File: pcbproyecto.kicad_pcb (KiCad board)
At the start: 4 copper layers, 75 x 108 mm, 21 parts, among them J1 Barrel_Jack_Switch, J2 Conn_02x20_Odd_Even, J3 Micro_SD_Card, J4 USB_A, J5 Conn_01x01_Male, P1 USB_C_Plug_USB2.0, U1 LM2576HVS-5, U2 LM117_TO3, U3 OSD3358-512M-BSM

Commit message: Progress
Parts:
- removed J5: Conn_01x01_Male, Connector_PinHeader_1.00mm:PinHeader_1x01_P1.00mm_Vertical
- added H1: MGT, MountingHole:MountingHole_3.2mm_M3, F.Cu at (81.3, 120.0)
- added H2: MGT, MountingHole:MountingHole_3.2mm_M3, F.Cu at (19.1, 119.0)
- added H3: MGT, MountingHole:MountingHole_3.2mm_M3, F.Cu at (17.9, 23.8)
- added H4: MGT, MountingHole:MountingHole_3.2mm_M3, F.Cu at (81.4, 23.9)
- added LED1: L_PWR, LED_SMD:LED_0603_1608Metric, F.Cu at (72.3, 71.9)
- added PWR1: PSH_BTN, footprints:MINI_PUSHBUTTON, F.Cu at (77.3, 71.1)
- added Q1: MMBT3906, Package_TO_SOT_SMD:SOT-23, F.Cu at (92.1, 99.8)
- added Q2: MMBT3906, Package_TO_SOT_SMD:SOT-23, F.Cu at (50.4, 38.2)
- added R1: 1K, Resistor_SMD:R_0603_1608Metric, F.Cu at (72.3, 67.7)
- added R2: 0.1 5%, Resistor_SMD:R_0603_1608Metric, F.Cu at (95.7, 100.0)
- added R3: R, Resistor_SMD:R_0603_1608Metric, F.Cu at (98.2, 100.0)
- added R4: R, Resistor_SMD:R_0603_1608Metric, F.Cu at (95.7, 96.0)
- added R5: R, Resistor_SMD:R_0603_1608Metric, F.Cu at (91.1, 91.1)
- added R6: R, Resistor_SMD:R_0603_1608Metric, F.Cu at (60.4, 39.9)
- added R7: R, Resistor_SMD:R_0603_1608Metric, F.Cu at (60.3, 36.3)
- added R8: R, Resistor_SMD:R_0603_1608Metric, F.Cu at (53.8, 38.2)
- added RST1: PSH_BTN, footprints:MINI_PUSHBUTTON, F.Cu at (77.3, 64.3)
- added TP1: TP_PWR_EN, TestPoint:TestPoint_Pad_1.0x1.0mm, F.Cu at (74.6, 56.8)
- added TP2: TP_PWRONSTN, TestPoint:TestPoint_Pad_1.0x1.0mm, F.Cu at (77.6, 56.8)
- added TP3: TP_WAKEUP, TestPoint:TestPoint_Pad_1.0x1.0mm, F.Cu at (74.6, 53.7)
- added TP4: TP_EXTINTN, TestPoint:TestPoint_Pad_1.0x1.0mm, F.Cu at (77.6, 53.7)
- added TP5: TP_I2C_SCL, TestPoint:TestPoint_Pad_1.0x1.0mm, F.Cu at (74.6, 50.7)
- added TP6: TP_I2C_SDA, TestPoint:TestPoint_Pad_1.0x1.0mm, F.Cu at (77.6, 50.7)
- added TP7: TP_VIN_BAT, TestPoint:TestPoint_Pad_1.0x1.0mm, F.Cu at (74.6, 47.6)
- added U4: TLVH431, Package_TO_SOT_SMD:SOT-23, F.Cu at (92.1, 95.3)
- added U5: TLVH431, Package_TO_SOT_SMD:SOT-23, F.Cu at (57.0, 38.2)
- C1: value 100u -> 100uF
- moved J2 19.3 mm to (35.9, 27.1), turned to 90 degrees
- turned U3 to 0 degrees
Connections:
- J2 pad 1: /UART_TX -> /Interfaces/UART_TX
- J2 pad 3: /UART_RX -> /Interfaces/UART_RX
- U3 pad A7: /Sistem In Package/ADC_VREF+ -> Net-(U3-PadA7)
- U3 pad A9: /Sistem In Package/ADC_VREF- -> Net-(U3-PadA9)
- U3 pad B7: /Sistem In Package/ADC_VREF+ -> Net-(U3-PadB7)
- U3 pad B9: /Sistem In Package/ADC_VREF- -> Net-(U3-PadB9)
- U3 pad C10: Net-(U3-PadC10) -> Net-(TP5-Pad1)
- U3 pad C11: Net-(U3-PadC11) -> Net-(TP6-Pad1)
- U3 pad D10: Net-(U3-PadD10) -> Net-(TP5-Pad1)
- U3 pad D11: Net-(U3-PadD11) -> Net-(TP6-Pad1)
- U3 pad D4: Net-(U3-PadD4) -> Net-(TP4-Pad1)
- U3 pad D8: Net-(U3-PadD8) -> GND
- U3 pad D9: Net-(U3-PadD9) -> GND
- U3 pad E10: Net-(U3-PadE10) -> GND
- U3 pad E11: Net-(U3-PadE11) -> GND
- U3 pad E12: Net-(U3-PadE12) -> GND
- U3 pad E4: Net-(U3-PadE4) -> Net-(TP4-Pad1)
- U3 pad E5: Net-(U3-PadE5) -> GND
- U3 pad E6: Net-(U3-PadE6) -> GND
- U3 pad E7: Net-(U3-PadE7) -> GND
- U3 pad E8: Net-(U3-PadE8) -> GND
- U3 pad E9: Net-(U3-PadE9) -> GND
- U3 pad F12: Net-(U3-PadF12) -> GND
- U3 pad F5: Net-(U3-PadF5) -> GND
- U3 pad G12: Net-(U3-PadG12) -> GND
- U3 pad G5: Net-(U3-PadG5) -> GND
- U3 pad H12: Net-(U3-PadH12) -> GND
- U3 pad H13: Net-(U3-PadH13) -> GND
- U3 pad H4: Net-(U3-PadH4) -> GND
- U3 pad H5: Net-(U3-PadH5) -> GND
- U3 pad J12: Net-(U3-PadJ12) -> GND
- U3 pad J13: Net-(U3-PadJ13) -> GND
- U3 pad J4: Net-(U3-PadJ4) -> GND
- U3 pad J5: Net-(U3-PadJ5) -> GND
- U3 pad K12: Net-(U3-PadK12) -> GND
- U3 pad K5: Net-(U3-PadK5) -> GND
- U3 pad L12: Net-(U3-PadL12) -> GND
- U3 pad L4: Net-(U3-PadL4) -> Net-(TP3-Pad1)
- U3 pad L5: Net-(U3-PadL5) -> GND
- U3 pad M10: Net-(U3-PadM10) -> GND
- U3 pad M11: Net-(U3-PadM11) -> GND
- U3 pad M12: Net-(U3-PadM12) -> GND
- U3 pad M4: Net-(U3-PadM4) -> Net-(TP3-Pad1)
- U3 pad M5: Net-(U3-PadM5) -> GND
- U3 pad M6: Net-(U3-PadM6) -> GND
- U3 pad M7: Net-(U3-PadM7) -> GND
- U3 pad M8: Net-(U3-PadM8) -> GND
- U3 pad M9: Net-(U3-PadM9) -> GND
- U3 pad N10: Net-(U3-PadN10) -> Net-(TP1-Pad1)
- U3 pad N11: Net-(U3-PadN11) -> Net-(TP1-Pad1)
- U3 pad N4: Net-(U3-PadN4) -> Net-(TP2-Pad1)
- U3 pad N5: Net-(U3-PadN5) -> Net-(TP2-Pad1)
- U3 pad N8: Net-(U3-PadN8) -> GND
- U3 pad N9: Net-(U3-PadN9) -> GND
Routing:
- net +3V3: track 197.8 -> 164.8 mm
- net /UART_TX: track 0.00 -> 33.0 mm
- net /UART_RX: track 0.00 -> 30.6 mm
- net VDD_5V: track 17.5 -> 0.00 mm, vias 0 -> 3
- net GND: track 404.3 -> 408.8 mm, vias 10 -> 18
- net Net-(U3-PadC14): track 0.00 -> 4.42 mm
- net Net-(U3-PadB15): track 0.00 -> 3.11 mm
- net Net-(U3-PadA15): track 0.00 -> 3.10 mm
- net Net-(U3-PadB14): track 0.00 -> 3.04 mm
- net Net-(U3-PadB13): track 0.00 -> 3.00 mm
- net Net-(U3-PadA16): track 0.00 -> 1.62 mm
- net Net-(U3-PadB16): track 0.00 -> 1.58 mm
- net Net-(U3-PadA14): track 0.00 -> 1.57 mm
- net Net-(TP2-Pad1): track 0.00 -> 1.27 mm
- net VDD_3V3A: track 0.00 -> 1.27 mm, vias 0 -> 3
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- added copper zone on F.Cu, net GND
- added copper zone on GND.Cu, net GND
- added copper zone on F.Cu, net USB_DC
- added copper zone on F.Cu, net VDD_3V3A
- added copper zone on F.Cu, net VDD_5V
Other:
- rule via_min_drill: 0.3048 -> 0.2
- rule via_min_size: 0.6096 -> 0.3048

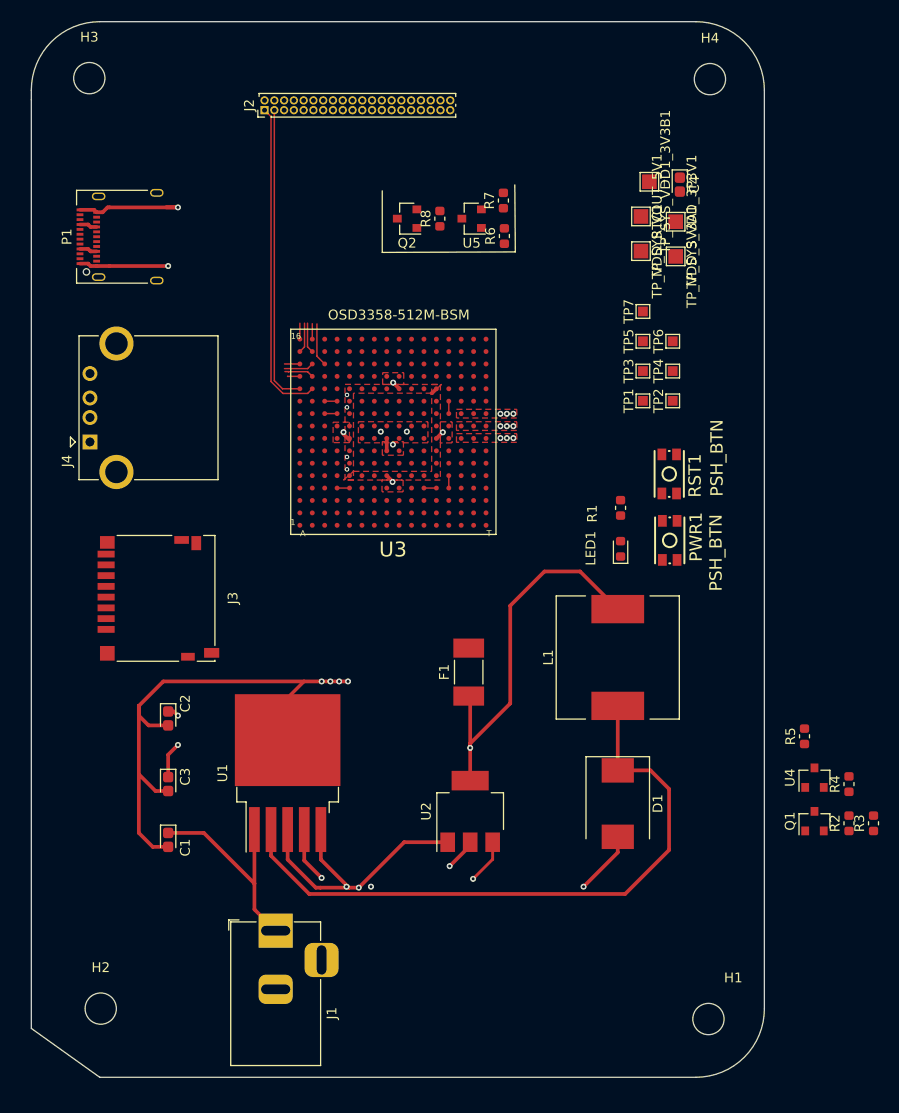
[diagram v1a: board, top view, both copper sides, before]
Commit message: EMD Protection
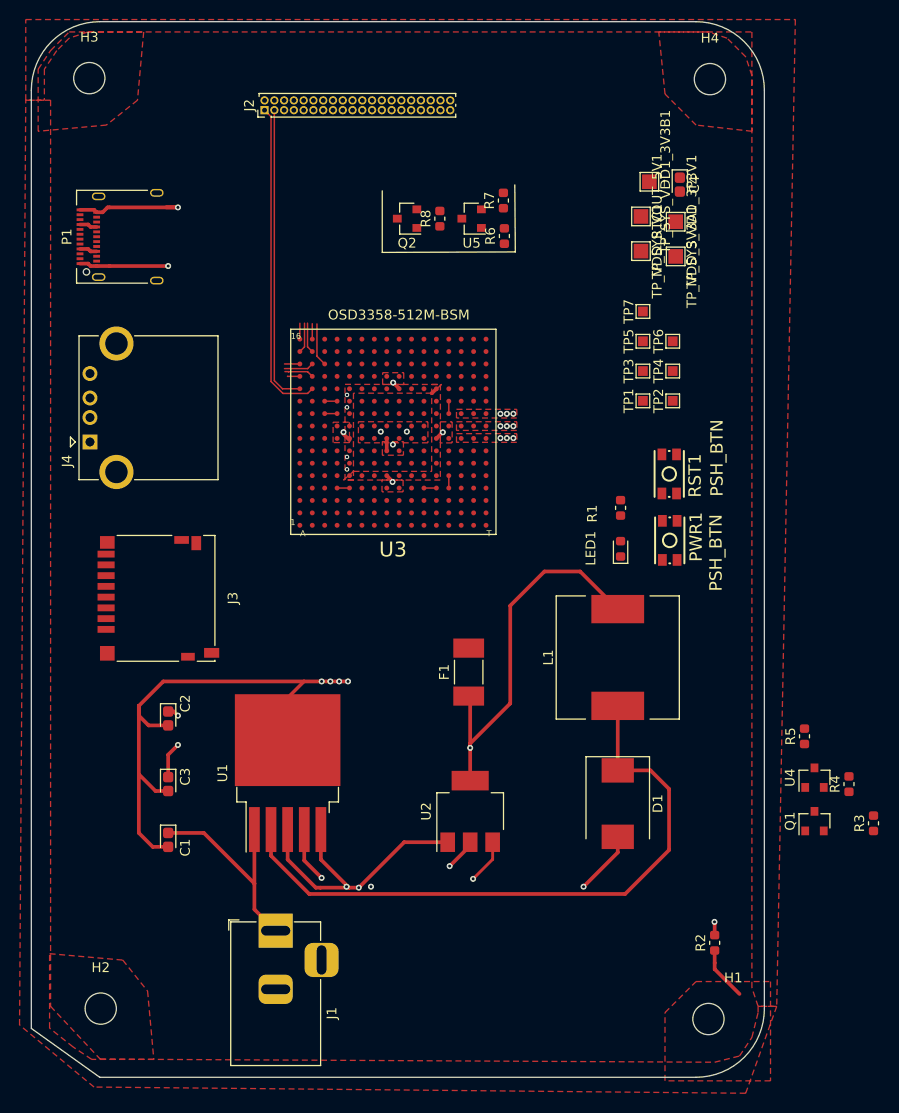
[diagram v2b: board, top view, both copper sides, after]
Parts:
- moved R2 18.4 mm to (81.9, 112.2)
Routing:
- net GND: track 408.8 -> 425.0 mm, vias 18 -> 19
- net CGND: track 0.00 -> 5.50 mm
- added copper zone on F.Cu, net CGND
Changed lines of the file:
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@@
     (thickness 1.6)
     (drawings 12)
-    (tracks 215)
+    (tracks 225)
     (zones 0)
     (modules 46)
@@
   )
   (setup
-    (last_trace_width 0.1524)
+    (last_trace_width 0.381)
     (user_trace_width 0.1524)
     (user_trace_width 0.381)
@@
   )
   (module Resistor_SMD:R_0603_1608Metric (layer F.Cu)
-    (at 95.6576 100.0144 90)
+    (at 81.915 112.2425 90)
     (descr "Resistor SMD 0603 (1608 Metric), square (rectangular) end terminal, IPC_7351 nominal, (Body size source: http://www.tortai-tech.com/upload/download/2011102023233369053.pdf), generated with kicad-footprint-generator")
     (tags resistor)
@@
       (effects (font (size 1 1) (thickness 0.15)))
     )
-    (fp_text value "0.1 5%" (at 0 1.43 90) (layer F.Fab)
+    (fp_text value "0.1 5%" (at 0 1.43 270) (layer F.Fab)
       (effects (font (size 1 1) (thickness 0.15)))
     )
@@
   (via (at 44.2976 62.5348) (size 0.4572) (drill 0.254) (layers F.Cu B.Cu) (net 1))
   (via (at 44.2976 63.8048) (size 0.4572) (drill 0.254) (layers F.Cu B.Cu) (net 1))
+  (segment (start 81.915 111.455) (end 81.915 110.315) (width 0.381) (layer F.Cu) (net 1))
+  (segment (start 81.915 110.315) (end 81.915 110.115) (width 0.381) (layer F.Cu) (net 1))
+  (via (at 81.9 110.1) (size 0.6096) (drill 0.3048) (layers F.Cu B.Cu) (net 1))
+  (segment (start 81.915 110.115) (end 81.9 110.1) (width 0.381) (layer F.Cu) (net 1))
+  (segment (start 68.5 106.6) (end 78.3 106.6) (width 0.381) (layer GND.Cu) (net 1))
+  (segment (start 78.4 106.6) (end 81.9 110.1) (width 0.381) (layer GND.Cu) (net 1))
+  (segment (start 78.3 106.6) (end 78.4 106.6) (width 0.381) (layer GND.Cu) (net 1))
   (segment (start 34.825 108.825) (end 38 112) (width 0.381) (layer F.Cu) (net 2))
   (segment (start 29.65 101) (end 34.825 106.175) (width 0.381) (layer F.Cu) (net 2))
@@
   (segment (start 42.015 58.09754) (end 43.285 58.09754) (width 0.1524) (layer F.Cu) (net 245))
   (segment (start 42.015 56.82754) (end 43.285 56.82754) (width 0.1524) (layer F.Cu) (net 246))
+  (segment (start 81.915 113.03) (end 81.915 114.3) (width 0.381) (layer F.Cu) (net 255))
+  (segment (start 81.915 114.3) (end 81.915 114.935) (width 0.381) (layer F.Cu) (net 255))
+  (segment (start 81.915 114.935) (end 84.455 117.475) (width 0.381) (layer F.Cu) (net 255))
   (zone (net 1) (net_name GND) (layer F.Cu) (hatch edge 0.508)
     (connect_pads yes (clearance 0.508))
@@
       )
     )
+  )
+  (zone (net 255) (net_name CGND) (layer F.Cu) (hatch edge 0.508)
+    (connect_pads yes (clearance 0.508))
+    (min_thickness 0.254)
+    (fill yes (arc_segments 32) (thermal_gap 0.508) (thermal_bridge_width 0.508))
+    (polygon
+      (pts
+        (xy 13.97 118.745) (xy 19.05 124.1425) (xy 81.915 124.46) (xy 84.455 123.825) (xy 85.725 121.92)
+        (xy 86.36 119.38) (xy 86.36 118.745) (xy 88.265 118.745) (xy 85.09 127.635) (xy 18.415 127)
+        (xy 10.795 120.65) (xy 11.43 26.035) (xy 13.97 26.035)
+      )
+    )
+  )
+  (zone (net 255) (net_name CGND) (layer F.Cu) (hatch edge 0.508)
+    (connect_pads yes (clearance 0.508))
+    (min_thickness 0.254)
+    (fill yes (arc_segments 32) (thermal_gap 0.508) (thermal_bridge_width 0.508))
+    (polygon
+      (pts
+        (xy 88.265 118.745) (xy 86.36 118.745) (xy 85.725 116.84) (xy 85.725 23.495) (xy 85.09 21.59)
+        (xy 83.185 19.685) (xy 81.28 19.05) (xy 17.78 19.05) (xy 15.875 19.685) (xy 14.605 20.955)
+        (xy 13.335 22.86) (xy 13.335 26.035) (xy 11.43 26.035) (xy 11.43 17.78) (xy 90.17 17.78)
+      )
+    )
+  )
+  (zone (net 255) (net_name CGND) (layer F.Cu) (hatch edge 0.508)
+    (connect_pads yes (clearance 0.508))
+    (min_thickness 0.254)
+    (fill yes (arc_segments 32) (thermal_gap 0.508) (thermal_bridge_width 0.508) (smoothing fillet) (radius 5))
+    (polygon
+      (pts
+        (xy 22.86 26.035) (xy 19.685 28.575) (xy 12.7 29.21) (xy 12.7 22.86) (xy 13.97 20.955)
+        (xy 15.875 19.05) (xy 23.495 19.05)
+      )
+    )
+  )
+  (zone (net 255) (net_name CGND) (layer F.Cu) (hatch edge 0.508)
+    (connect_pads yes (clearance 0.508))
+    (min_thickness 0.254)
+    (fill yes (arc_segments 32) (thermal_gap 0.508) (thermal_bridge_width 0.508) (smoothing fillet) (radius 5))
+    (polygon
+      (pts
+        (xy 85.725 29.21) (xy 80.01 28.575) (xy 76.835 25.4) (xy 76.2 19.05) (xy 85.725 19.05)
+      )
+    )
+  )
+  (zone (net 255) (net_name CGND) (layer F.Cu) (hatch edge 0.508)
+    (connect_pads yes (clearance 0.508))
+    (min_thickness 0.254)
+    (fill yes (arc_segments 32) (thermal_gap 0.508) (thermal_bridge_width 0.508) (smoothing fillet) (radius 5))
+    (polygon
+      (pts
+        (xy 76.835 126.365) (xy 76.835 119.38) (xy 80.01 116.205) (xy 87.63 116.205) (xy 87.63 126.365)
+      )
+    )
+  )
+  (zone (net 255) (net_name CGND) (layer F.Cu) (hatch edge 0.508)
+    (connect_pads yes (clearance 0.508))
+    (min_thickness 0.254)
+    (fill yes (arc_segments 32) (thermal_gap 0.508) (thermal_bridge_width 0.508) (smoothing fillet) (radius 5))
+    (polygon
+      (pts
+        (xy 21.355229 114.009418) (xy 23.895229 117.184418) (xy 24.530229 124.169418) (xy 18.180229 124.169418) (xy 16.275229 122.899418)
+        (xy 13.8684 120.97512) (xy 13.8684 113.35512)
+      )
+    )

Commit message: Progress
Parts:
- removed J2: Conn_02x20_Odd_Even, Connector_PinHeader_1.00mm:PinHeader_2x20_P1.00mm_Vertical
- removed J4: USB_A, Connector_USB:USB_A_CONNFLY_DS1095-WNR0
- removed P1: USB_C_Plug_USB2.0, Connector_USB:USB_C_Receptacle_Amphenol_12401610E4-2A
- removed the R1 at (72.3, 67.7)
- removed RST1: PSH_BTN, footprints:MINI_PUSHBUTTON
- removed TP1: TP_PWR_EN, TestPoint:TestPoint_Pad_1.0x1.0mm
- removed TP2: TP_PWRONSTN, TestPoint:TestPoint_Pad_1.0x1.0mm
- removed TP3: TP_WAKEUP, TestPoint:TestPoint_Pad_1.0x1.0mm
- removed TP4: TP_EXTINTN, TestPoint:TestPoint_Pad_1.0x1.0mm
- removed TP5: TP_I2C_SCL, TestPoint:TestPoint_Pad_1.0x1.0mm
- removed TP6: TP_I2C_SDA, TestPoint:TestPoint_Pad_1.0x1.0mm
- removed TP7: TP_VIN_BAT, TestPoint:TestPoint_Pad_1.0x1.0mm
- removed TP_SYS_VDD1_3V3B1, TP_SYS_VDD_3P3V1, TP_SYS_VOUT_5V1, TP_VDD_3V3A1, TP_VDD_RTC1: TestPoint, TestPoint:TestPoint_Pad_1.5x1.5mm
- added C5: 100uF, Capacitor_Tantalum_SMD:CP_EIA-1608-08_AVX-J, F.Cu at (30.7, 102.9)
- added C6: 100u, Capacitor_Tantalum_SMD:CP_EIA-1608-08_AVX-J, F.Cu at (30.7, 100.2)
- added C7: 1000u, Capacitor_Tantalum_SMD:CP_EIA-1608-08_AVX-J, F.Cu at (30.7, 97.5)
- added C8: 10uF, 10V, Capacitor_Tantalum_SMD:CP_EIA-1608-08_AVX-J, F.Cu at (62.0, 71.5)
- added C9: 0.1uF 6,3V, Capacitor_Tantalum_SMD:CP_EIA-1608-08_AVX-J, F.Cu at (62.0, 75.6)
- added IC1: SN74LVC1G07DCK, Package_TO_SOT_SMD:SOT-23-5, F.Cu at (73.2, 48.1)
- added J5: USB_B_Micro, Connector_USB:USB_Micro-B_Amphenol_10104110_Horizontal, F.Cu at (19.3, 56.5)
- added R2: R, Resistor_SMD:R_0603_1608Metric, F.Cu at (62.7, 33.7)
- added R22: 1K, Resistor_SMD:R_0603_1608Metric, F.Cu at (70.0, 34.8)
- added R23: 1M , 1%, Resistor_SMD:R_0603_1608Metric, F.Cu at (48.1, 27.0)
- added R9: 100K, pocketbeagle:RN0804, F.Cu at (44.6, 77.2)
- added RN1: 10K, pocketbeagle:RN0804, F.Cu at (34.5, 76.8)
- added RN2: 10K, pocketbeagle:RN0804, F.Cu at (34.5, 74.3)
- C1: value 100uF -> 0.1uF , 6.3V
- C2: value 1000u -> 18pF, 50V
- C3: value 100u -> 18pF, 50V
- J3: value Micro_SD_Card -> USB_A; footprint Connector_Card:microSD_HC_Hirose_DM3D-SF -> Connector_USB:USB_A_CONNFLY_DS1095-WNR0
- Q2: value MMBT3906 -> 24 MHz; footprint Package_TO_SOT_SMD:SOT-23 -> Crystal:Crystal_SMD_TXC_7A-2Pin_5x3.2mm
- R5: value R -> 10K
- R6, R7, R8: value R -> 100K; footprint Resistor_SMD:R_0603_1608Metric -> pocketbeagle:RN0804
- U1: value LM2576HVS-5 -> TLVH431; footprint Package_TO_SOT_SMD:TO-263-5_TabPin3 -> Package_TO_SOT_SMD:SOT-23
- U2: value LM117_TO3 -> OSD3358-512M-BSM; footprint Package_TO_SOT_SMD:SOT-223-3_TabPin2 -> footprints:OSD335X-BGA-256
- U3: value OSD3358-512M-BSM -> LM117_TO3; footprint footprints:OSD335X-BGA-256 -> Package_TO_SOT_SMD:SOT-223-3_TabPin2
- U4: value TLVH431 -> LM2576HVS-5; footprint Package_TO_SOT_SMD:SOT-23 -> Package_TO_SOT_SMD:TO-263-5_TabPin3
- U5: value TLVH431 -> MICROSD; footprint Package_TO_SOT_SMD:SOT-23 -> pocketbeagle:MICROSD
- moved R3 78.1 mm to (62.7, 30.4), turned to 0 degrees
- moved Q1 77.7 mm to (67.5, 26.1), turned to 0 degrees
- moved R4 76.5 mm to (62.7, 27.0), turned to 0 degrees
- moved C1 75.0 mm to (78.7, 48.4), turned to 90 degrees
- moved C3 68.5 mm to (48.1, 31.2), turned to 180 degrees
- moved R5 67.3 mm to (48.2, 39.2), turned to 180 degrees
- moved U1 66.2 mm to (56.2, 31.2), turned to 0 degrees
- moved C2 59.1 mm to (48.2, 34.5), turned to 180 degrees
- moved C4 53.3 mm to (34.1, 64.5), turned to 90 degrees
- moved U5 47.3 mm to (29.7, 76.7)
- moved R7 41.3 mm to (53.0, 76.9), turned to 0 degrees
- moved U4 39.8 mm to (52.4, 98.0)
- moved R8 39.6 mm to (47.4, 77.2), turned to 0 degrees
- moved J3 39.1 mm to (28.2, 38.0)
- moved R6 37.2 mm to (56.0, 76.9), turned to 0 degrees
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- renumbered R2 to R1
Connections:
- C1 pad 1: /Power Suply/in_pwr_supply -> GND
- C1 pad 2: GND -> VDD_RTC
- C2 pad 1: +5V -> /Sistem In Package/OSC_OUT
- C2 pad 2: GND -> /Sistem In Package/OSC_GND
- C3 pad 1: +3V3 -> /Sistem In Package/OSC_IN
- C3 pad 2: GND -> /Sistem In Package/OSC_GND
- C4 pad 1: /Sistem In Package/ADC_VREF+ -> /Sistem In Package/VREF+
- C4 pad 2: /Sistem In Package/ADC_VREF- -> /Sistem In Package/VREF-
- J1 pad 1: /Power Suply/in_pwr_supply -> /Interfaces/IN_PWR_SUPPLY
- J3 pad 1: Net-(J3-Pad1) -> /USB1_VBU
- J3 pad 2: Net-(J3-Pad2) -> /USB1_D-
- J3 pad 3: Net-(J3-Pad3) -> /USB1_D+
- J3 pad 4: Net-(J3-Pad4) -> GND
- J3 pad 5: Net-(J3-Pad5) -> CGND
- PWR1 pad 3: Net-(PWR1-Pad3) -> /Interfaces/PWR_ON
- PWR1 pad 4: Net-(PWR1-Pad3) -> /Interfaces/PWR_ON
- Q2 pad 1: Net-(Q2-Pad1) -> /Sistem In Package/OSC_OUT
- Q2 pad 2: VDD_3V3B -> /Sistem In Package/OSC_IN
- R3 pad 1: VDD_3V3B -> VDD_RTC
- R3 pad 2: Net-(R3-Pad2) -> Net-(R2-Pad2)
- R4 pad 1: VDD_RTC -> Net-(Q1-Pad1)
- R4 pad 2: Net-(R3-Pad2) -> VDD_3V3B
- R5 pad 1: Net-(Q1-Pad1) -> Net-(R5-Pad1)
- R5 pad 2: VDD_3V3B -> GND
- R6 pad 1: VDD_3V3B -> GND
- R6 pad 2: Net-(R6-Pad2) -> GND
- R7 pad 1: VDD_RTC -> GND
- R7 pad 2: Net-(R6-Pad2) -> GND
- R8 pad 1: Net-(Q2-Pad1) -> VDD_3V3B
- R8 pad 2: VDD_3V3B -> GND
- U1 pad 1: /Power Suply/in_pwr_supply -> Net-(Q1-Pad1)
- U1 pad 2: Net-(D1-Pad1) -> Net-(R2-Pad2)
- U1 pad 3: GND -> VDD_RTC
- U4 pad 1: Net-(Q1-Pad1) -> /Interfaces/IN_PWR_SUPPLY
- U4 pad 2: Net-(R3-Pad2) -> Net-(D1-Pad1)
- U4 pad 3: VDD_RTC -> GND
- U5 pad 1: Net-(Q2-Pad1) -> /Interfaces/MMC0_DAT2
- U5 pad 2: Net-(R6-Pad2) -> /Interfaces/MMC0_DAT3
- U5 pad 3: VDD_RTC -> /Interfaces/MMC0_CMD
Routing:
- net GND: track 425.0 -> 131.5 mm, vias 19 -> 22
- net +3V3: track 164.8 -> 13.0 mm, vias 2 -> 0
- net +5V: track 221.8 -> 79.5 mm, vias 4 -> 0
- net VDD_3V3B: track 0.00 -> 129.2 mm, vias 0 -> 3
- net CGND: track 5.50 -> 98.0 mm, vias 0 -> 1
- net VDD_RTC: track 0.00 -> 86.9 mm, vias 0 -> 4
- net /Interfaces/PWR_ON: track 0.00 -> 51.1 mm
- net USB_DC: track 3.61 -> 53.6 mm, vias 3 -> 5
- net VDD_5V: track 0.00 -> 45.0 mm, vias 3 -> 7
- net /USB0_D-: track 0.00 -> 42.4 mm
- net /USB0_D+: track 0.00 -> 42.4 mm
- net /USB0_ID: track 0.00 -> 42.0 mm
- net /Interfaces/MMC0_DAT2: track 0.00 -> 40.3 mm, vias 0 -> 2
- net /Sistem In Package/OSC_OUT: track 0.00 -> 40.3 mm, vias 0 -> 2
- net Net-(D1-Pad1): track 65.8 -> 27.0 mm
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- added copper zone on F.Cu, net SYS_5V
- added copper zone on F.Cu, net VDD_1V8
- added copper zone on F.Cu, net VDD_3V3AUX
- added copper zone on F.Cu, net VDD_3V3B
- added copper zone on F.Cu, net VDD_RTC
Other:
- net class USB added: clearance 0.1, trace_width 0.1524, via_dia 0.6096, via_drill 0.3048
- board text added: "Clock"
- board text added: "Powerdown - Clamping"
- board text added: "Rev 1 Alessandro Ghezzo UTN FRBA - TD 2"
